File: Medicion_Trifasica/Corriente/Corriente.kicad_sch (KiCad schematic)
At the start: 25 parts, among them IC1 AMS1117-3.3, J1 XADC_Input, J2 Screw_Terminal_01x02, J3 XADC_Ref, J4 POWER, U1 ACS725xLCTR-20AB, U2 LM358

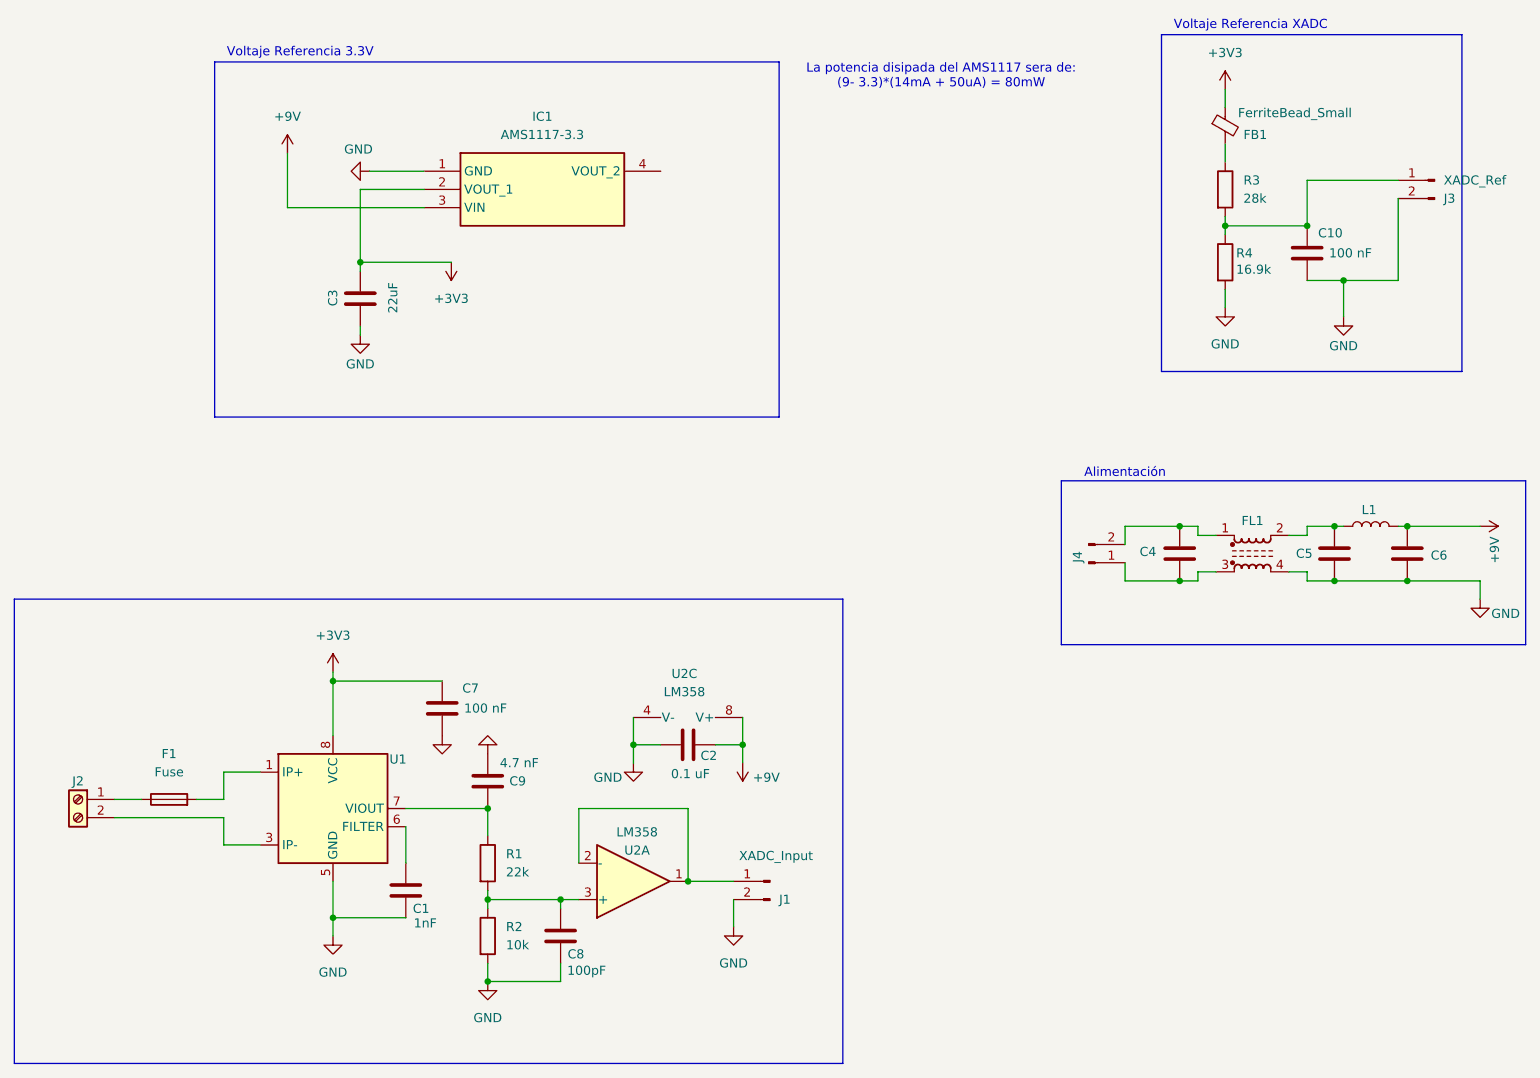
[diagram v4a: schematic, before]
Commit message: Mejora en la organizacion de los circuitos con netclases y colores
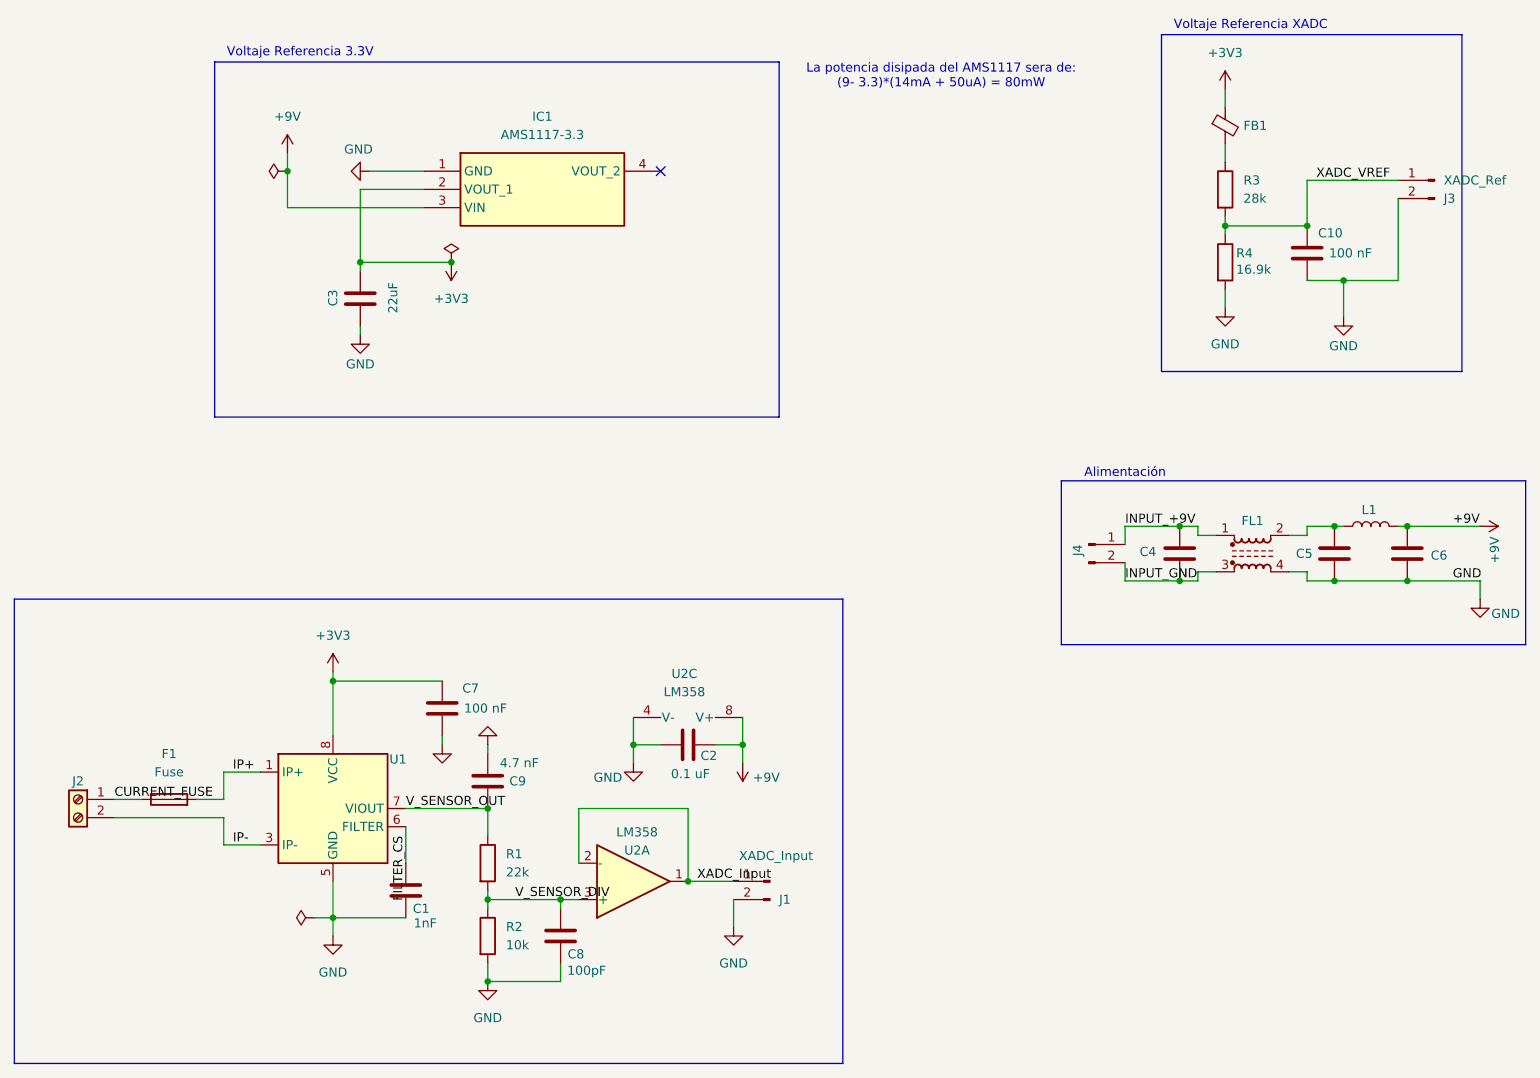
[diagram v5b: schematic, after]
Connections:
- net XADC_VREF: now reaches C10.1, J3.1 (Pin_1), R3.2, R4.1
- net V_SENSOR_OUT: now reaches C9.1, R1.1, U1.7 (VIOUT)
- net V_SENSOR_DIV: now reaches C8.2, R1.2, R2.1, U2.3 (+)
- net FILTER_CS: now reaches C1.2, U1.6 (FILTER)
- net XADC_Input: now reaches J1.1 (Pin_1), U2.1, U2.2 (-)
- net IP+: now reaches F1.2, U1.1 (IP+), U1.2 (IP+)
- net IP-: now reaches J2.2 (Pin_2), U1.3 (IP-), U1.4 (IP-)
- net INPUT_GND: now reaches C4.2, FL1.3
- net INPUT_GND: now also J4.2 (Pin_2); no longer J4.1 (Pin_1)
- net INPUT_+9V: now reaches C4.1, FL1.1
- net INPUT_+9V: now also J4.1 (Pin_1); no longer J4.2 (Pin_2)
- net CURRENT_FUSE: now reaches F1.1, J2.1 (Pin_1)
- no-connect marks 0 -> 1

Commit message: Mejoras y trabajos realizadps
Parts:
- removed FL1: Choke_CommonMode_FerriteCore_1234, Inductor_THT:Choke_EPCOS_B82722A, symbol Filter:Choke_CommonMode_FerriteCore_1234
- C1, C8, C9: footprint Capacitor_SMD:C_01005_0402Metric_Pad0.57x0.30mm_HandSolder -> Capacitor_SMD:C_1206_3216Metric_Pad1.33x1.80mm_HandSolder
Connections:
- net INPUT_GND is gone; now on net GND: C4.2, J4.2 (Pin_2)
- net INPUT_+9V: now also C5.2, L1.1
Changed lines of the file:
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@@
-	(wire
-		(pts
-			(xy 199.39 101.6) (xy 199.39 102.87)
-		)
-		(stroke
-			(width 0)
-			(type default)
-		)
-	)
 	(wire
 		(pts
@@
 	(wire
 		(pts
-			(xy 199.39 102.87) (xy 203.2 102.87)
-		)
-		(stroke
-			(width 0)
-			(type default)
-		)
-	)
-	(wire
-		(pts
 			(xy 212.09 60.96) (xy 204.47 60.96)
 		)
@@
 	(wire
 		(pts
-			(xy 186.69 101.6) (xy 184.15 101.6)
-		)
-		(stroke
-			(width 0)
-			(type default)
-		)
-	)
-	(wire
-		(pts
 			(xy 67.31 58.42) (xy 67.31 59.69)
 		)
@@
 	(wire
 		(pts
-			(xy 196.85 96.52) (xy 199.39 96.52)
-		)
-		(stroke
-			(width 0)
-			(type default)
-		)
-	)
-	(wire
-		(pts
 			(xy 85.09 138.43) (xy 85.09 134.62)
 		)
@@
 	(wire
 		(pts
-			(xy 184.15 102.87) (xy 181.61 102.87)
+			(xy 181.61 102.87) (xy 203.2 102.87)
 		)
 		(stroke
@@
 	(wire
 		(pts
-			(xy 199.39 95.25) (xy 203.2 95.25)
-		)
-		(stroke
-			(width 0)
-			(type default)
-		)
-	)
-	(wire
-		(pts
 			(xy 63.5 144.78) (xy 63.5 149.86)
 		)
@@
 	(wire
 		(pts
-			(xy 184.15 96.52) (xy 186.69 96.52)
-		)
-		(stroke
-			(width 0)
-			(type default)
-		)
-	)
-	(wire
-		(pts
 			(xy 63.5 149.86) (xy 73.66 149.86)
 		)
@@
 	(wire
 		(pts
-			(xy 196.85 101.6) (xy 199.39 101.6)
-		)
-		(stroke
-			(width 0)
-			(type default)
-		)
-	)
-	(wire
-		(pts
 			(xy 120.65 125.73) (xy 120.65 121.92)
 		)
@@
 	(wire
 		(pts
-			(xy 184.15 101.6) (xy 184.15 102.87)
-		)
-		(stroke
-			(width 0)
-			(type default)
-		)
-	)
-	(wire
-		(pts
 			(xy 116.84 125.73) (xy 120.65 125.73)
 		)
@@
 	(wire
 		(pts
-			(xy 184.15 96.52) (xy 184.15 95.25)
-		)
-		(stroke
-			(width 0)
-			(type default)
-		)
-	)
-	(wire
-		(pts
-			(xy 199.39 96.52) (xy 199.39 95.25)
-		)
-		(stroke
-			(width 0)
-			(type default)
-		)
-	)
-	(wire
-		(pts
 			(xy 80.01 58.42) (xy 67.31 58.42)
 		)
@@
 	(wire
 		(pts
-			(xy 184.15 95.25) (xy 181.61 95.25)
+			(xy 181.61 95.25) (xy 203.2 95.25)
 		)
 		(stroke
@@
 		)
 	)
-	(label "INPUT_GND"
-		(at 173.99 102.87 0)
-		(effects
-			(font
-				(size 1.27 1.27)
-			)
-			(justify left bottom)
-		)
-	)
 	(label "XADC_VREF"
 		(at 200.66 46.99 0)
@@
 			)
 		)
-		(property "Footprint" "Capacitor_SMD:C_01005_0402Metric_Pad0.57x0.30mm_HandSolder"
+		(property "Footprint" "Capacitor_SMD:C_1206_3216Metric_Pad1.33x1.80mm_HandSolder"
 			(at 94.2848 148.59 0)
 			(effects
@@
 			)
 		)
-		(property "Footprint" "Capacitor_SMD:C_01005_0402Metric_Pad0.57x0.30mm_HandSolder"
+		(property "Footprint" "Capacitor_SMD:C_1206_3216Metric_Pad1.33x1.80mm_HandSolder"
 			(at 72.6948 142.24 0)
 			(effects
@@
 			)
 		)
-		(property "Footprint" "Capacitor_SMD:C_01005_0402Metric_Pad0.57x0.30mm_HandSolder"
+		(property "Footprint" "Capacitor_SMD:C_1206_3216Metric_Pad1.33x1.80mm_HandSolder"
 			(at 84.1248 127 0)
 			(effects
@@
 					(unit 1)
 				)
-			)
-		)
-	)
-	(symbol
-		(lib_id "Filter:Choke_CommonMode_FerriteCore_1234")
-		(at 191.77 99.06 0)
-		(unit 1)
-		(exclude_from_sim no)
-		(in_bom yes)
-		(on_board yes)
-		(dnp no)
-		(property "Reference" "FL1"
-			(at 191.77 94.488 0)
-			(effects
-				(font
-					(size 1.27 1.27)
-				)
-			)
-		)
-		(property "Value" "Choke_CommonMode_FerriteCore_1234"
-			(at 191.643 93.98 0)
-			(effects
-				(font
-					(size 1.27 1.27)
-				)
-				(hide yes)
-			)
-		)
-		(property "Footprint" "Inductor_THT:Choke_EPCOS_B82722A"
-			(at 191.77 105.41 0)
-			(effects
-				(font
-					(size 1.27 1.27)
-				)
-				(hide yes)
-			)
-		)
-		(property "Datasheet" "~"
-			(at 191.77 107.315 0)
-			(effects
-				(font
-					(size 1.27 1.27)
-				)
-				(hide yes)
-			)
-		)
-		(property "Description" "Generic common-mode choke, ferrite core, 1234 pin order"
-			(at 191.77 99.06 0)
-			(effects
-				(font
-					(size 1.27 1.27)
-				)
-				(hide yes)
-			)
-		)
-		(pin "2"
-		)
-		(pin "1"
-		)
-		(pin "4"
-		)
-		(pin "3"
-		)
-		(instances
-			(project "Corriente"
-				(path "/cf53253e-7788-4c16-b67b-c1a8de54435a"
-					(reference "FL1")
-					(unit 1)
-				)
